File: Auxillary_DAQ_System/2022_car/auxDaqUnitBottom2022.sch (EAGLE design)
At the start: 85 parts, among them IC1 ADS8332IBPWR, IC2 ADS8332IBPWR, IC3 ADS8332IBPWR, IC4 XBEE, IC6 REG_3V3_LM3940, U1 REF5040AIDR

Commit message: Working on board files
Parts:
- R27, R28, R29: value (none) -> 10k
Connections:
- net 30: now also R1.1
- net 31: no longer R1.1
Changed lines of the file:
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@@
 <part name="+3V5" library="GTOR - Documation Frame" deviceset="+3V3" device=""/>
 <part name="+3V6" library="GTOR - Documation Frame" deviceset="+3V3" device=""/>
-<part name="R27" library="GTOR - Passive Components" deviceset="RES_SMD" device="R0603" package3d_urn="urn:adsk.eagle:package:23555/3"/>
-<part name="R28" library="GTOR - Passive Components" deviceset="RES_SMD" device="R0603" package3d_urn="urn:adsk.eagle:package:23555/3"/>
-<part name="R29" library="GTOR - Passive Components" deviceset="RES_SMD" device="R0603" package3d_urn="urn:adsk.eagle:package:23555/3"/>
+<part name="R27" library="GTOR - Passive Components" deviceset="RES_SMD" device="R0603" package3d_urn="urn:adsk.eagle:package:23555/3" value="10k"/>
+<part name="R28" library="GTOR - Passive Components" deviceset="RES_SMD" device="R0603" package3d_urn="urn:adsk.eagle:package:23555/3" value="10k"/>
+<part name="R29" library="GTOR - Passive Components" deviceset="RES_SMD" device="R0603" package3d_urn="urn:adsk.eagle:package:23555/3" value="10k"/>
 <part name="+3V7" library="GTOR - Documation Frame" deviceset="+3V3" device=""/>
 <part name="+3V8" library="GTOR - Documation Frame" deviceset="+3V3" device=""/>
@@
 <label x="170.18" y="99.06" size="1.27" layer="95" rot="R180" xref="yes"/>
 </segment>
+<segment>
+<pinref part="R1" gate="G$1" pin="1"/>
+<wire x1="162.56" y1="68.58" x2="160.02" y2="68.58" width="0.1524" layer="91"/>
+<label x="160.02" y="68.58" size="1.27" layer="95" rot="R180" xref="yes"/>
+</segment>
 </net>
 <net name="31" class="0">
@@
 <wire x1="177.8" y1="96.52" x2="170.18" y2="96.52" width="0.1524" layer="91"/>
 <label x="170.18" y="96.52" size="1.27" layer="95" rot="R180" xref="yes"/>
-</segment>
-<segment>
-<pinref part="R1" gate="G$1" pin="1"/>
-<wire x1="162.56" y1="68.58" x2="160.02" y2="68.58" width="0.1524" layer="91"/>
-<label x="160.02" y="68.58" size="1.27" layer="95" rot="R180" xref="yes"/>
 </segment>
 </net>
@@
 <plain>
 <text x="43.18" y="172.72" size="5.08" layer="97">XBee</text>
-<wire x1="91.44" y1="185.42" x2="91.44" y2="101.6" width="0.1524" layer="94"/>
-<wire x1="91.44" y1="101.6" x2="68.58" y2="101.6" width="0.1524" layer="94"/>
+<wire x1="81.28" y1="185.42" x2="81.28" y2="101.6" width="0.1524" layer="94"/>
+<wire x1="81.28" y1="101.6" x2="68.58" y2="101.6" width="0.1524" layer="94"/>
 <text x="22.86" y="83.82" size="5.08" layer="97">Headers</text>
 <wire x1="68.58" y1="101.6" x2="0" y2="101.6" width="0.1524" layer="94"/>

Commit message: Completed auxDAQ rev1
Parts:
- added JP8: (no value), GTOR - Connectors:PINHD-1X3
- added JP9: (no value), GTOR - Connectors:PINHD-1X22
- renumbered U$3 to U3, U$4 to U4, U$5 to U5, U$6 to U6, U$7 to U7, U$8 to U8
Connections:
- removed net 18: JP2.9, U$1.18-A4/SDA0
- removed net 19: JP2.8, U$1.19-A5/SCL0
- removed net CS=3: IC1.FS/!CS, JP1.5, U$1.3-LRCLK2
- removed net CS=4: IC2.FS/!CS, JP1.6, U$1.4-BCLK2
- removed net CS=5: IC3.FS/!CS, JP1.7, U$1.5-IN2
- new net 3: JP1.5, JP9.3, U$1.3-LRCLK2
- new net 4: JP1.6, JP9.4, U$1.4-BCLK2
- new net 5: JP1.7, JP9.5, U$1.5-IN2
- new net SCL: JP2.8, JP9.21, U$1.19-A5/SCL0
- new net SDA: JP2.9, JP9.22, U$1.18-A4/SDA0
- net +3V3: now also JP8.2
- net +5V: now also JP8.3
- net 2: now also JP9.2
- net 24: now also JP9.16
- net 25: now also JP9.17
- net 26: now also JP9.8
- net 27: now also JP9.9
- net 28: now also JP9.10
- net 29: now also JP9.11
- net 30: now also JP9.1
- net 31: now also JP9.12
- net 32: now also JP9.13
- net 33: now also IC1.FS/!CS
- net 34: now also IC2.FS/!CS
- net 35: now also IC3.FS/!CS
- net 6: now also JP9.6
- net 7: now also JP9.7
- net 8: now also JP9.14
- net 9: now also JP9.15
- net GND: now also JP2.2, JP8.1
- net MISO: now also JP9.20; no longer IC3.SDI
- net MOSI: now also IC3.SDI, JP9.19; no longer JP2.2
- net SCK: now also JP9.18
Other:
- moved on the sheet: JP1, JP2, JP3

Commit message: Minor DRC fixes and trace thickening
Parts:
- JP3: device GTOR - Connectors:PINHD-1X3 -> GTOR - Connectors:PINHD-1X2
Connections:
- net +5V: no longer JP3.3
- net GND: no longer U$1.GND4, U$1.GND5
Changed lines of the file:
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@@
 <part name="JP1" library="GTOR - Connectors" deviceset="PINHD-1X24" device="" package3d_urn="urn:adsk.eagle:package:22448/2"/>
 <part name="JP2" library="GTOR - Connectors" deviceset="PINHD-1X24" device="" package3d_urn="urn:adsk.eagle:package:22448/2"/>
-<part name="JP3" library="GTOR - Connectors" deviceset="PINHD-1X3" device="" package3d_urn="urn:adsk.eagle:package:22458/2"/>
-<part name="P+4" library="GTOR - Documation Frame" deviceset="+5V" device=""/>
 <part name="+3V2" library="GTOR - Documation Frame" deviceset="+3V3" device=""/>
 <part name="SUPPLY4" library="GTOR - Documation Frame" deviceset="GND" device=""/>
@@
 <part name="SUPPLY17" library="GTOR - Documation Frame" deviceset="GND" device=""/>
 <part name="JP9" library="GTOR - Connectors" deviceset="PINHD-1X22" device="" package3d_urn="urn:adsk.eagle:package:22442/3"/>
+<part name="JP3" library="GTOR - Connectors" deviceset="PINHD-1X2" device="" package3d_urn="urn:adsk.eagle:package:22435/2"/>
 </parts>
 <sheets>
@@
 <attribute name="VALUE" x="123.19" y="157.48" size="1.778" layer="96" rot="R180"/>
 </instance>
-<instance part="JP3" gate="A" x="132.08" y="66.04" smashed="yes" rot="R180">
-<attribute name="NAME" x="138.43" y="60.325" size="1.778" layer="95" rot="R180"/>
-<attribute name="VALUE" x="138.43" y="73.66" size="1.778" layer="96" rot="R180"/>
-</instance>
-<instance part="P+4" gate="1" x="142.24" y="76.2" smashed="yes">
-<attribute name="VALUE" x="142.24" y="71.12" size="1.778" layer="96" rot="R180"/>
-</instance>
 <instance part="+3V2" gate="G$1" x="144.78" y="71.12" smashed="yes">
 <attribute name="VALUE" x="144.78" y="66.04" size="1.778" layer="96" rot="R180"/>
@@
 <attribute name="NAME" x="179.07" y="95.885" size="1.778" layer="95" rot="R180"/>
 <attribute name="VALUE" x="179.07" y="157.48" size="1.778" layer="96" rot="R180"/>
+</instance>
+<instance part="JP3" gate="G$1" x="132.08" y="66.04" smashed="yes" rot="R180">
+<attribute name="NAME" x="138.43" y="60.325" size="1.778" layer="95" rot="R180"/>
+<attribute name="VALUE" x="138.43" y="71.12" size="1.778" layer="96" rot="R180"/>
 </instance>
 </instances>
@@
 </segment>
 <segment>
-<pinref part="U$1" gate="G$1" pin="GND4"/>
-<wire x1="53.34" y1="71.12" x2="53.34" y2="66.04" width="0.1524" layer="91"/>
-<label x="53.34" y="66.04" size="1.27" layer="95" rot="R270" xref="yes"/>
-</segment>
-<segment>
-<pinref part="U$1" gate="G$1" pin="GND5"/>
-<wire x1="55.88" y1="71.12" x2="55.88" y2="66.04" width="0.1524" layer="91"/>
-<label x="55.88" y="66.04" size="1.27" layer="95" rot="R270" xref="yes"/>
-</segment>
-<segment>
 <pinref part="U$1" gate="G$1" pin="GND6"/>
 <wire x1="58.42" y1="71.12" x2="58.42" y2="66.04" width="0.1524" layer="91"/>
@@
 </segment>
 <segment>
-<pinref part="JP3" gate="A" pin="1"/>
 <pinref part="SUPPLY4" gate="GND" pin="GND"/>
 <wire x1="134.62" y1="63.5" x2="142.24" y2="63.5" width="0.1524" layer="91"/>
 <wire x1="142.24" y1="63.5" x2="142.24" y2="60.96" width="0.1524" layer="91"/>
+<pinref part="JP3" gate="G$1" pin="1"/>
 </segment>
 <segment>
@@
 </segment>
 <segment>
-<pinref part="JP3" gate="A" pin="3"/>
-<pinref part="P+4" gate="1" pin="+5V"/>
-<wire x1="134.62" y1="68.58" x2="142.24" y2="68.58" width="0.1524" layer="91"/>
-<wire x1="142.24" y1="68.58" x2="142.24" y2="73.66" width="0.1524" layer="91"/>
-</segment>
-<segment>
 <pinref part="U$1" gate="G$1" pin="VIN"/>
 <wire x1="55.88" y1="162.56" x2="55.88" y2="165.1" width="0.1524" layer="91"/>
@@
 </segment>
 <segment>
-<pinref part="JP3" gate="A" pin="2"/>
 <pinref part="+3V2" gate="G$1" pin="+3V3"/>
 <wire x1="134.62" y1="66.04" x2="144.78" y2="66.04" width="0.1524" layer="91"/>
 <wire x1="144.78" y1="66.04" x2="144.78" y2="68.58" width="0.1524" layer="91"/>
-</segment>
-<segment>
+<pinref part="JP3" gate="G$1" pin="2"/>
+</segment>
+<segment>

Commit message: Just a bit of work I did on Tuesday
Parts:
- removed JP7: (no value), GTOR - Connectors:PINHD-1X8
- added A0, A1, A10, A11, A2, A3, A4, A5, A6, A7, A8, A9, D1, D2, D3, D4, D5, D6, D7, D8: (no value), GTOR - Microfit Connector:HEADER_POS3_43650-0300
- added CS=10, CS=11: (no value), GTOR - Microfit Connector:HEADER_POS6_43045-0600
- added I2C1, I2C2: (no value), GTOR - Microfit Connector:HEADER_POS4_43045-0401
- JP6: device GTOR - Connectors:PINHD-1X8 -> GTOR - Connectors:PINHD-1X4
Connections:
- new net 10: CS=10.2
- new net 11: CS=11.2
- net +3V3: now also CS=10.1, CS=11.1, D1.1, D2.1, D3.1, D4.1, D5.1, D6.1, D7.1, D8.1, I2C1.1, I2C2.1
- net +5V: now also A0.1, A1.1, A10.1, A11.1, A2.1, A3.1, A4.1, A5.1, A6.1, A7.1, A8.1, A9.1
- net 2: now also D1.2
- net 3: now also D2.2
- net 4: now also D3.2
- net 5: now also D4.2
- net 6: now also D5.2
- net 7: now also D6.2
- net 8: now also D7.2
- net 9: now also D8.2
- net ADC1: now also A0.2; no longer JP7.1
- net ADC10: now also A9.2; no longer JP6.2
- net ADC11: now also A10.2; no longer JP6.3
- net ADC12: now also A11.2; no longer JP6.4
- net ADC13: now also JP6.1; no longer JP6.5
- net ADC14: now also JP6.2; no longer JP6.6
- net ADC15: now also JP6.3; no longer JP6.7
- net ADC16: now also JP6.4; no longer JP6.8
- net ADC2: now also A1.2; no longer JP7.2
- net ADC3: now also A2.2; no longer JP7.3
- net ADC4: now also A3.2; no longer JP7.4
- net ADC5: now also A4.2; no longer JP7.5
- net ADC6: now also A5.2; no longer JP7.6
- net ADC7: now also A6.2; no longer JP7.7
- net ADC8: now also A7.2; no longer JP7.8
- net ADC9: now also A8.2; no longer JP6.1
- net GND: now also A0.3, A1.3, A10.3, A11.3, A2.3, A3.3, A4.3, A5.3, A6.3, A7.3, A8.3, A9.3, CS=10.6, CS=11.6, D1.3, D2.3, D3.3, D4.3, D5.3, D6.3, D7.3, D8.3, I2C1.4, I2C2.4
- net MISO: now also CS=10.4, CS=11.4
- net MOSI: now also CS=10.3, CS=11.3
- net SCK: now also CS=10.5, CS=11.5
- net SCL: now also I2C1.3, I2C2.3
- net SDA: now also I2C1.2, I2C2.2
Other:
- note added: "Analog Pins"
- note added: "Digital Pins"
- note added: "I2C"
- note added: "SPI"

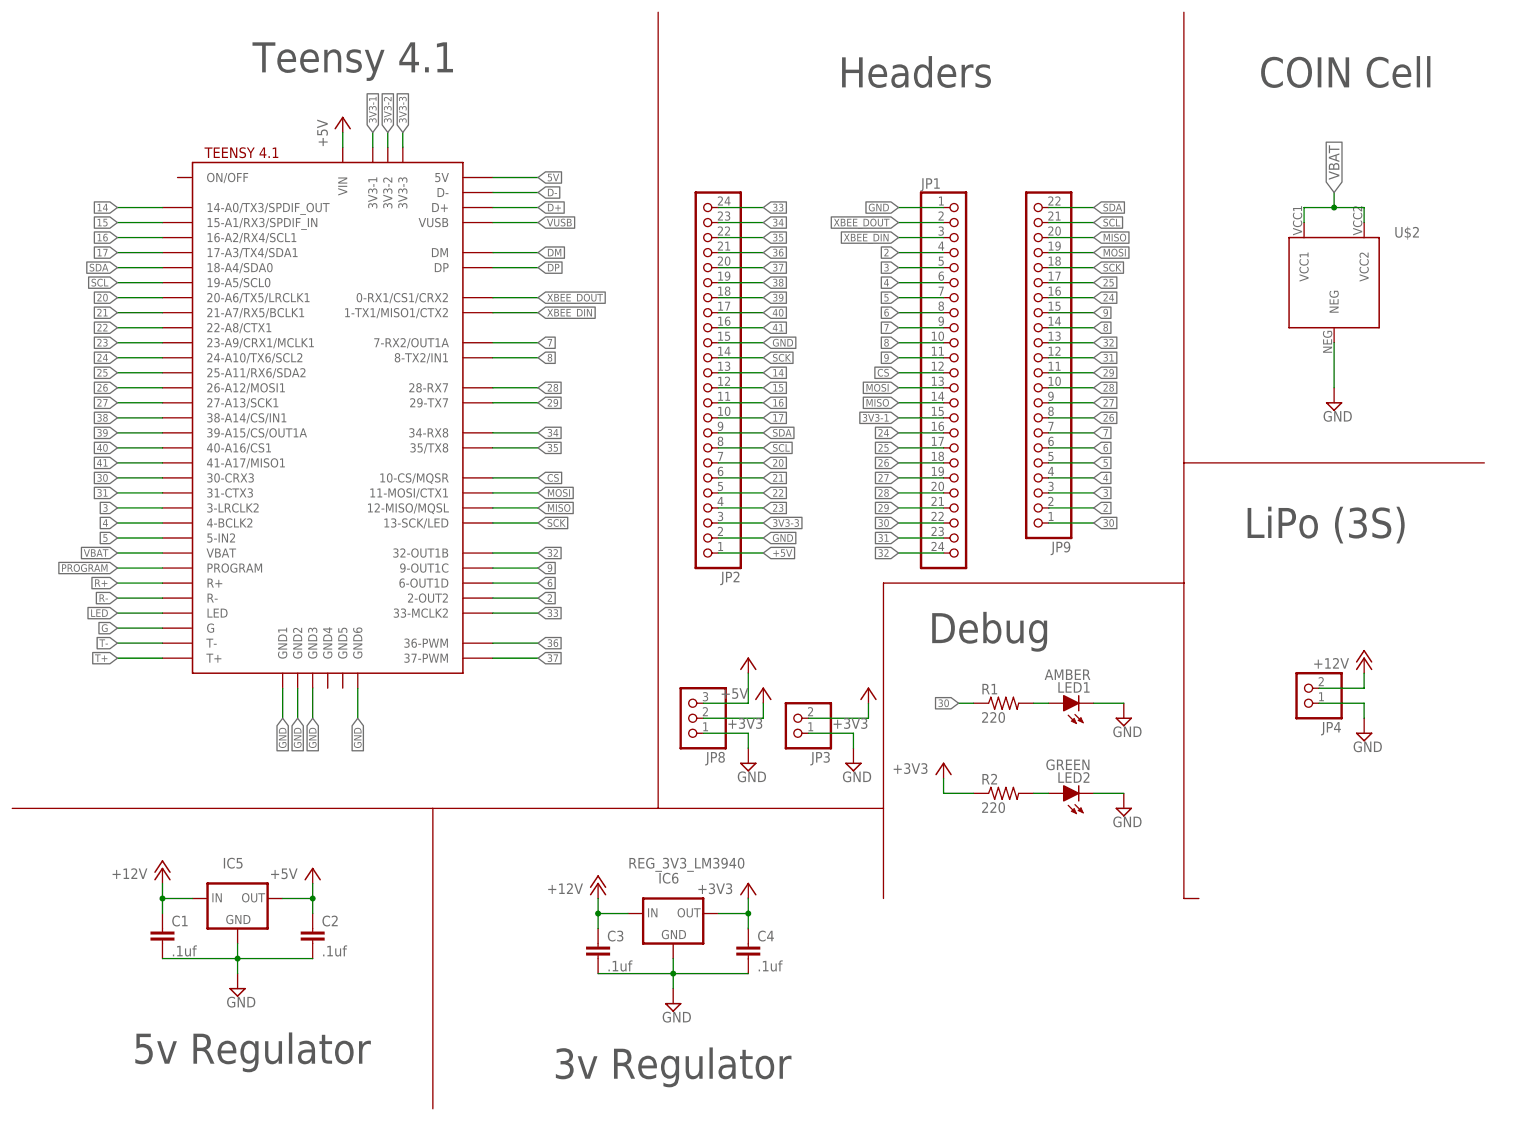
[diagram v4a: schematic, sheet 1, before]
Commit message: Bottom board has some airwires, but everything should line up
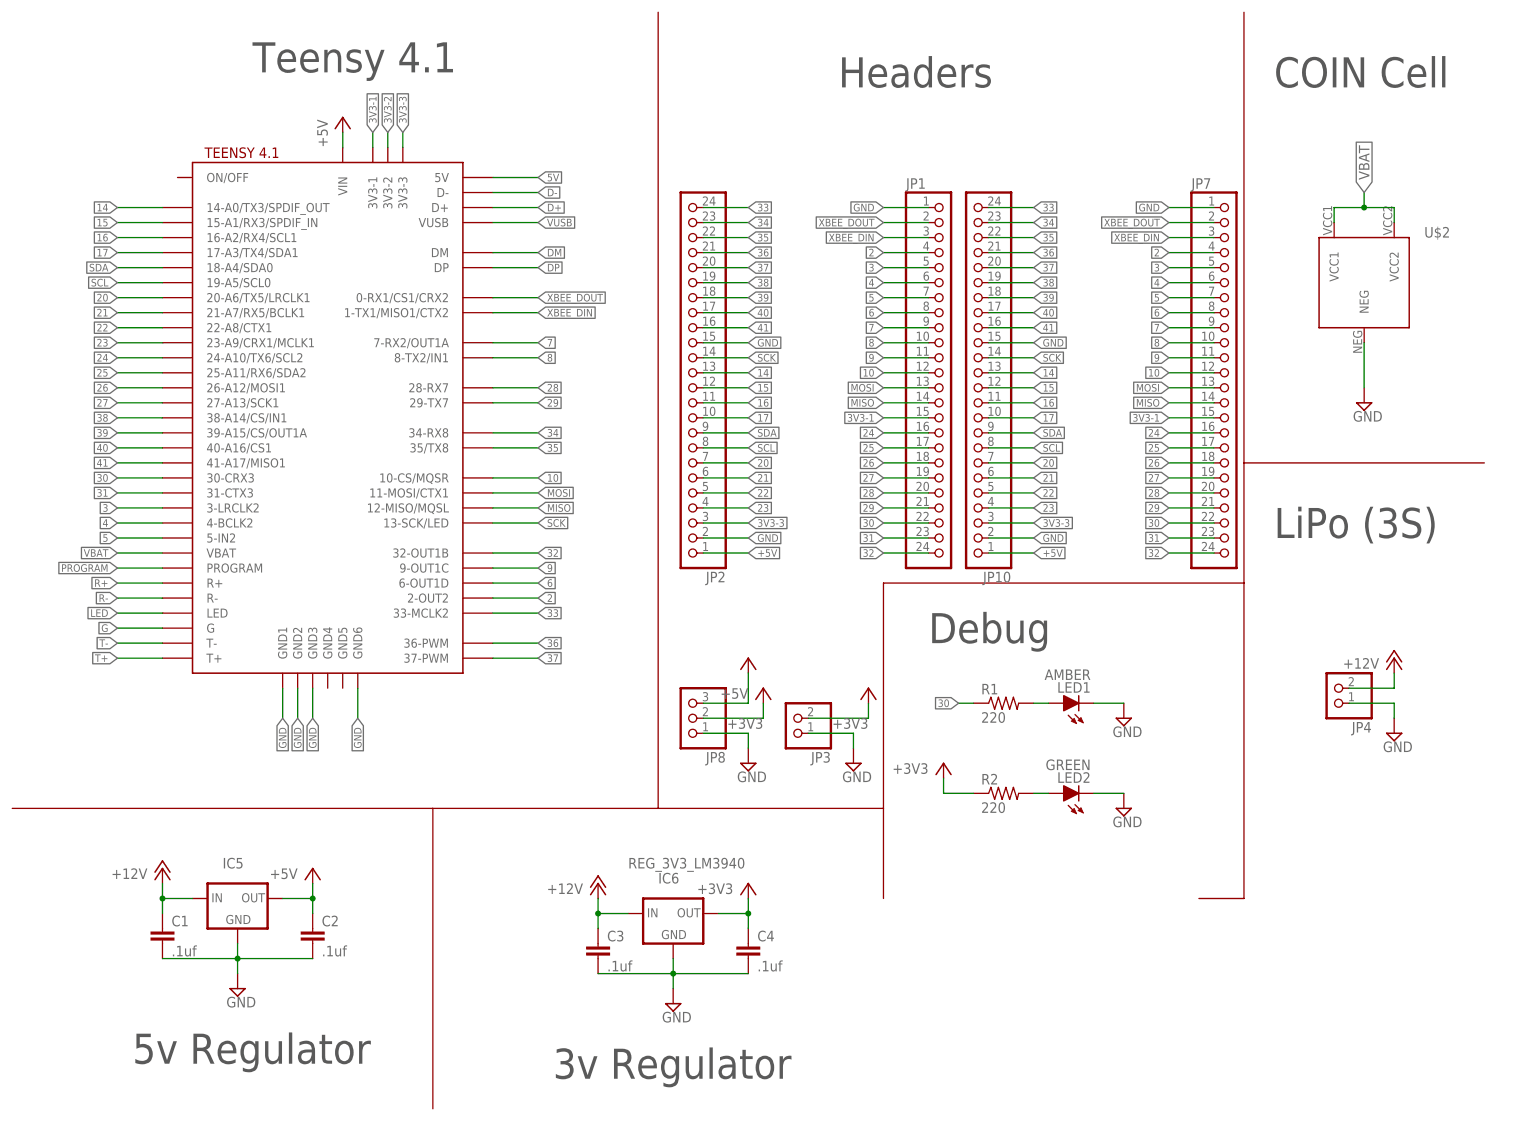
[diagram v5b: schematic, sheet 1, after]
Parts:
- removed JP9: (no value), GTOR - Connectors:PINHD-1X22
- added JP10, JP7: (no value), GTOR - Connectors:PINHD-1X24
- added R30, R31, R32: 10k, GTOR - Passive Components:RES_SMDR0603
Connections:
- removed net 11: CS=11.2
- removed net CS: JP1.12, U$1.10-CS/MQSR
- new net N$25: IC3.!CONVST, R30.1
- new net N$30: IC1.!CONVST, R31.1
- new net N$35: IC2.!CONVST, R32.1
- net +5V: now also JP10.1
- net 10: now also CS=10.5, JP1.12, JP7.12, U$1.10-CS/MQSR; no longer CS=10.2
- net 14: now also CS=11.5, JP10.13
- net 15: now also JP10.12
- net 16: now also JP10.11
- net 17: now also JP10.10
- net 2: now also JP7.4; no longer JP9.2
- net 20: now also JP10.7
- net 21: now also JP10.6
- net 22: now also JP10.5
- net 23: now also JP10.4
- net 24: now also JP7.16; no longer JP9.16
- net 25: now also JP7.17; no longer JP9.17
- net 26: now also JP7.18; no longer JP9.8
- net 27: now also JP7.19; no longer JP9.9
- net 28: now also JP7.20; no longer JP9.10
- net 29: now also JP7.21; no longer JP9.11
- net 3: now also JP7.5; no longer JP9.3
- net 30: now also JP7.22; no longer JP9.1
- net 31: now also JP7.23; no longer JP9.12
- net 32: now also JP7.24; no longer JP9.13
- net 33: now also JP10.24
- net 34: now also JP10.23
- net 35: now also JP10.22
- net 36: now also JP10.21
- net 37: now also JP10.20
- net 38: now also JP10.19
- net 39: now also JP10.18
- net 3V3-1: now also JP7.15
- net 3V3-3: now also JP10.3
- net 4: now also JP7.6; no longer JP9.4
- net 40: now also JP10.17
- net 41: now also JP10.16
- net 5: now also JP7.7; no longer JP9.5
- net 6: now also JP7.8; no longer JP9.6
- net 7: now also JP7.9; no longer JP9.7
- net 8: now also JP7.10; no longer JP9.14
- net 9: now also JP7.11; no longer JP9.15
- net GND: now also JP10.15, JP10.2, JP7.1, R30.2, R31.2, R32.2
- net MISO: now also CS=10.3, CS=11.3, JP7.14; no longer CS=10.4, CS=11.4, JP9.20
- net MOSI: now also CS=10.2, CS=11.2, JP7.13; no longer CS=10.3, CS=11.3, JP9.19
- net SCK: now also CS=10.4, CS=11.4, JP10.14; no longer CS=10.5, CS=11.5, JP9.18
- net SCL: now also JP10.8; no longer JP9.21
- net SDA: now also JP10.9; no longer JP9.22
- net XBEE_DIN: now also JP7.3
- net XBEE_DOUT: now also JP7.2
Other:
- moved on the sheet: JP1, JP2, JP4, U$2

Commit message: Mostly done with Aux Daq Rework
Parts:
- added C33, C34, C35, C36, C37, C38: (no value), GTOR - Passive Components:CAP_SMDC0603
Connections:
- net +3V3: now also C36.1, C37.1, C38.1
- net +5V: now also C33.1, C34.1, C35.1
- net ADC1: no longer C5.1
- net ADC10: no longer C14.1
- net ADC11: now also U5.IN4+; no longer C15.1, U5.IN3+
- net ADC12: now also U5.IN3+; no longer C16.1, U5.IN4+
- net ADC13: now also U6.IN2+; no longer C17.1, U6.IN1+
- net ADC14: now also U6.IN1+; no longer C18.1, U6.IN2+
- net ADC15: no longer C19.1
- net ADC16: no longer C20.1
- net ADC17: no longer C21.1
- net ADC18: no longer C22.1
- net ADC19: now also U7.IN4+; no longer C23.1, U7.IN3+
- net ADC2: no longer C6.1
- net ADC20: now also U7.IN3+; no longer C24.1, U7.IN4+
- net ADC21: now also U8.IN2+; no longer C25.1, U8.IN1+
- net ADC22: now also U8.IN1+; no longer C26.1, U8.IN2+
- net ADC23: no longer C27.1
- net ADC24: no longer C28.1
- net ADC3: now also U3.IN4+; no longer C7.1, U3.IN3+
- net ADC4: now also U3.IN3+; no longer C8.1, U3.IN4+
- net ADC5: now also U4.IN2+; no longer C9.1, U4.IN1+
- net ADC6: now also U4.IN1+; no longer C10.1, U4.IN2+
- net ADC7: no longer C11.1
- net ADC8: no longer C12.1
- net ADC9: no longer C13.1
- net GND: now also C33.2, C34.2, C35.2, C36.2, C37.2, C38.2
- net IN1: now also C5.1
- net IN10: now also C14.1
- net IN11: now also C15.1, R12.2; no longer R13.2
- net IN12: now also C16.1, R13.2; no longer R12.2
- net IN13: now also C17.1, R18.1; no longer R15.1
- net IN14: now also C18.1, R15.1; no longer R18.1
- net IN15: now also C19.1
- net IN16: now also C20.1
- net IN17: now also C21.1
- net IN18: now also C22.1
- net IN19: now also C23.1, R20.2; no longer R21.2
- net IN2: now also C6.1
- net IN20: now also C24.1, R21.2; no longer R20.2
- net IN21: now also C25.1, R26.1; no longer R23.1
- net IN22: now also C26.1, R23.1; no longer R26.1
- net IN23: now also C27.1
- net IN24: now also C28.1
- net IN3: now also C7.1, R4.2; no longer R5.2
- net IN4: now also C8.1, R5.2; no longer R4.2
- net IN5: now also C9.1, R10.1; no longer R7.1
- net IN6: now also C10.1, R7.1; no longer R10.1
- net IN7: now also C11.1
- net IN8: now also C12.1
- net IN9: now also C13.1
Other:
- moved on the sheet: C30, C31, C32
